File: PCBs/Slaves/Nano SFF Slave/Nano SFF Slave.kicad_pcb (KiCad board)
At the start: 2 copper layers, 52.4 x 50 mm, 52 parts, among them J1 Screw_Terminal_01x02, J10 AVR-ISP-6, J11 Conn_01x06_Female, J12 Screw_Terminal_01x02, J13 Screw_Terminal_01x02, J14 Screw_Terminal_01x02, J15 Screw_Terminal_01x02, J16 Screw_Terminal_01x02, J2 Screw_Terminal_01x02, J3 Screw_Terminal_01x02, J4 Screw_Terminal_01x02, J5 Screw_Terminal_01x02, J6 Screw_Terminal_01x02, J7 Screw_Terminal_01x02, J8 Screw_Terminal_01x02, J9 Screw_Terminal_01x02, SW1 SW_DIP_x02, SW2 SW_DIP_x02, SW3 SW_MEC_5E, U1 ATmega328P-AU, U2 MAX487ESA+T, U3 ULN2003A, U4 MAX487CPA+, U5 AMS1117-5.0, Y1 Crystal_GND24

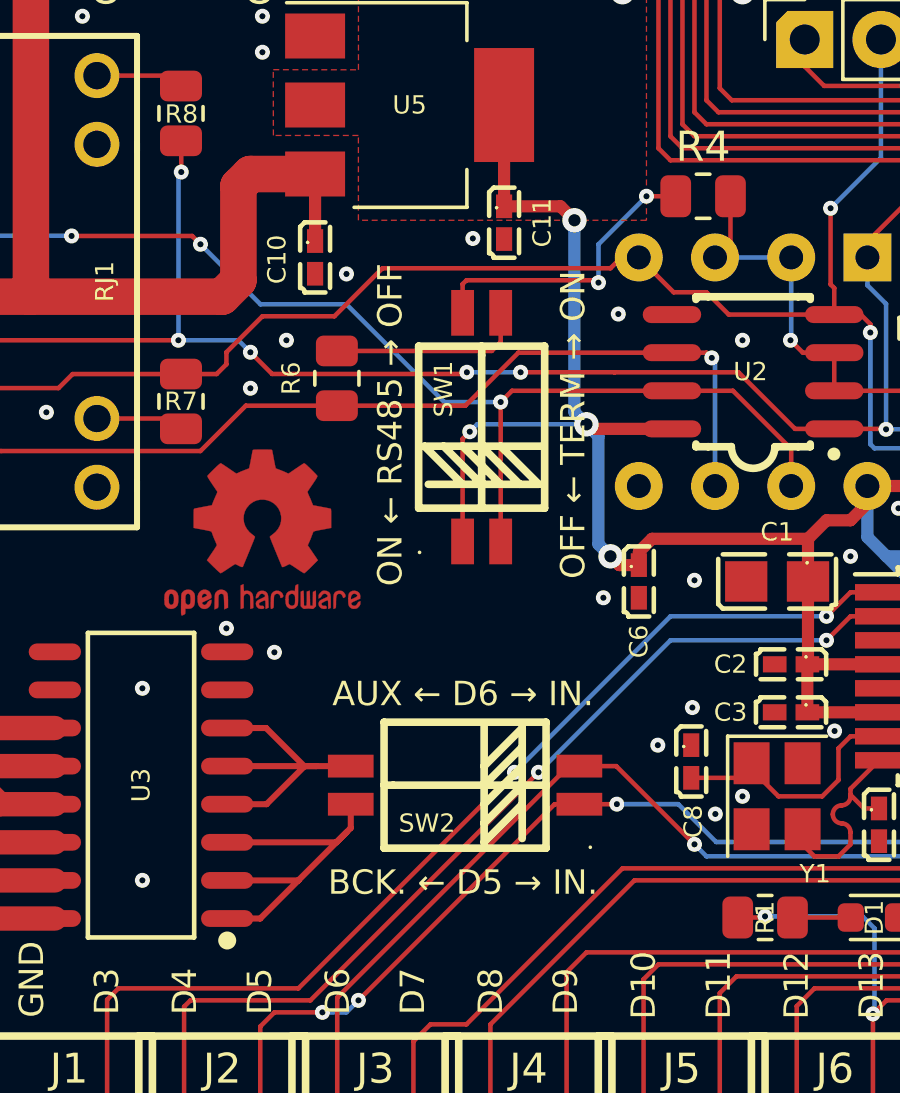
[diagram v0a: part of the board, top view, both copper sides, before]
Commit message: Updated Nano SFF Slave RS485 Switch and Silkscreen
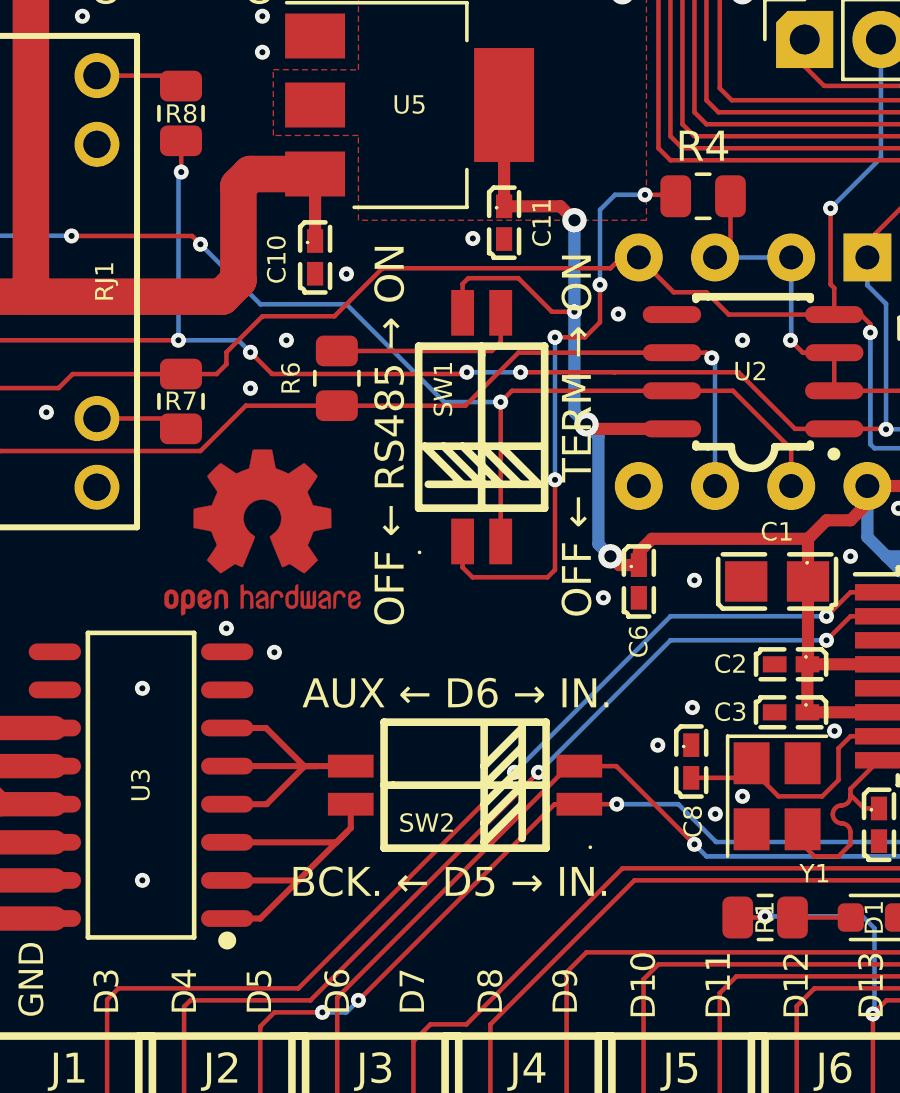
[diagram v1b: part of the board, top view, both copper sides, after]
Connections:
- R4 pad 1: Net-(SW1-Pad4) -> Net-(R4-Pad1)
- SW1 pad 1: +5V -> Net-(R4-Pad1)
- SW1 pad 4: Net-(SW1-Pad4) -> +5V
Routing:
- net Net-(R4-Pad1): track 0.00 -> 20.1 mm, vias 0 -> 4
- net Net-(SW1-Pad4): track 10.1 -> 0.00 mm, vias 2 -> 0
- net +5V: track 115.6 -> 113.1 mm
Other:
- board text added: "OFF ← RS485 → ON"
- board text removed: "ON ← RS485 → OFF"

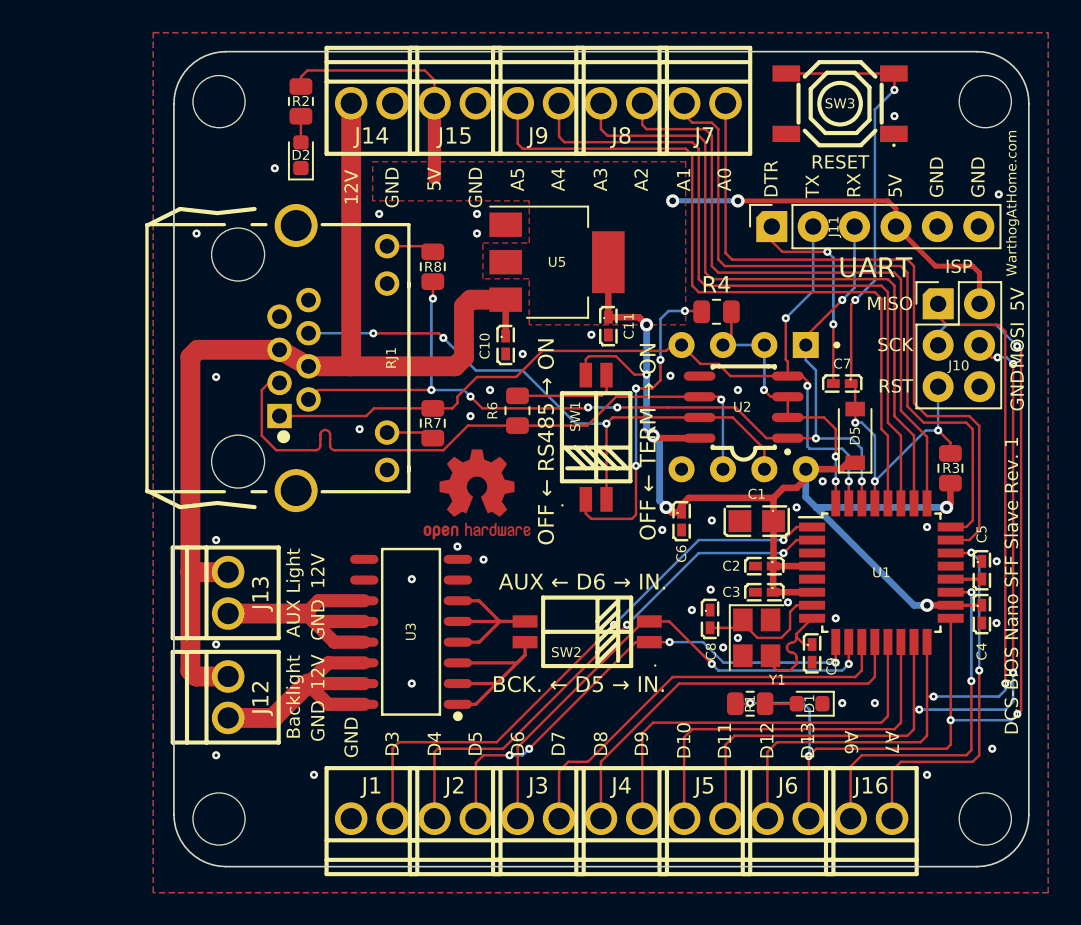
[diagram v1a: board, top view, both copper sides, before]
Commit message: Improved Nano SFF Silkscreen
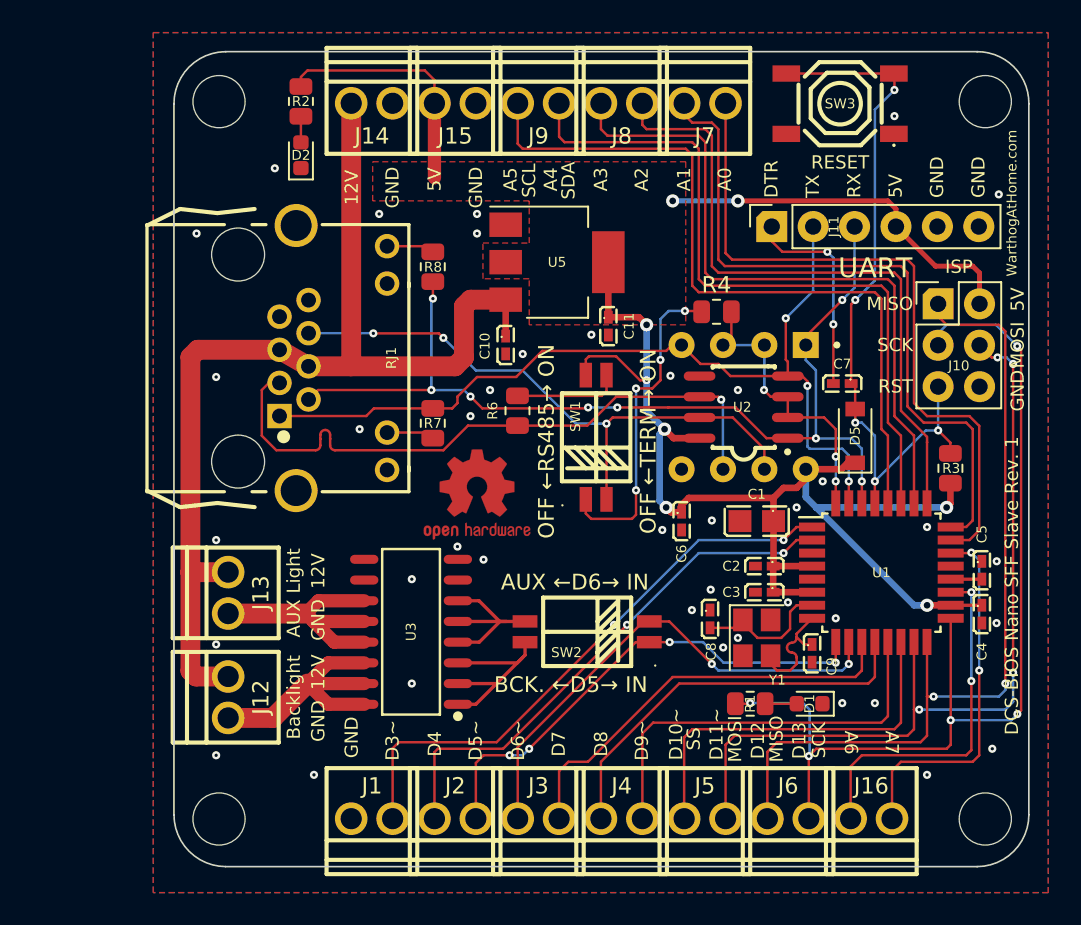
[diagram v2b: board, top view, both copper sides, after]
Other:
- board text added: "AUX ←D6→ IN"
- board text added: "BCK. ←D5→ IN"
- board text added: "OFF ←RS485→ ON"
- board text added: "OFF ←TERM→ ON"
- board text removed: "AUX ← D6 → IN."
- board text removed: "BCK. ← D5 → IN."
- board text removed: "OFF ← RS485 → ON"
- board text removed: "OFF ← TERM → ON"

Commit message: Nano SFF with DS4560S-AR+ hotplug protection (Not Orderable)
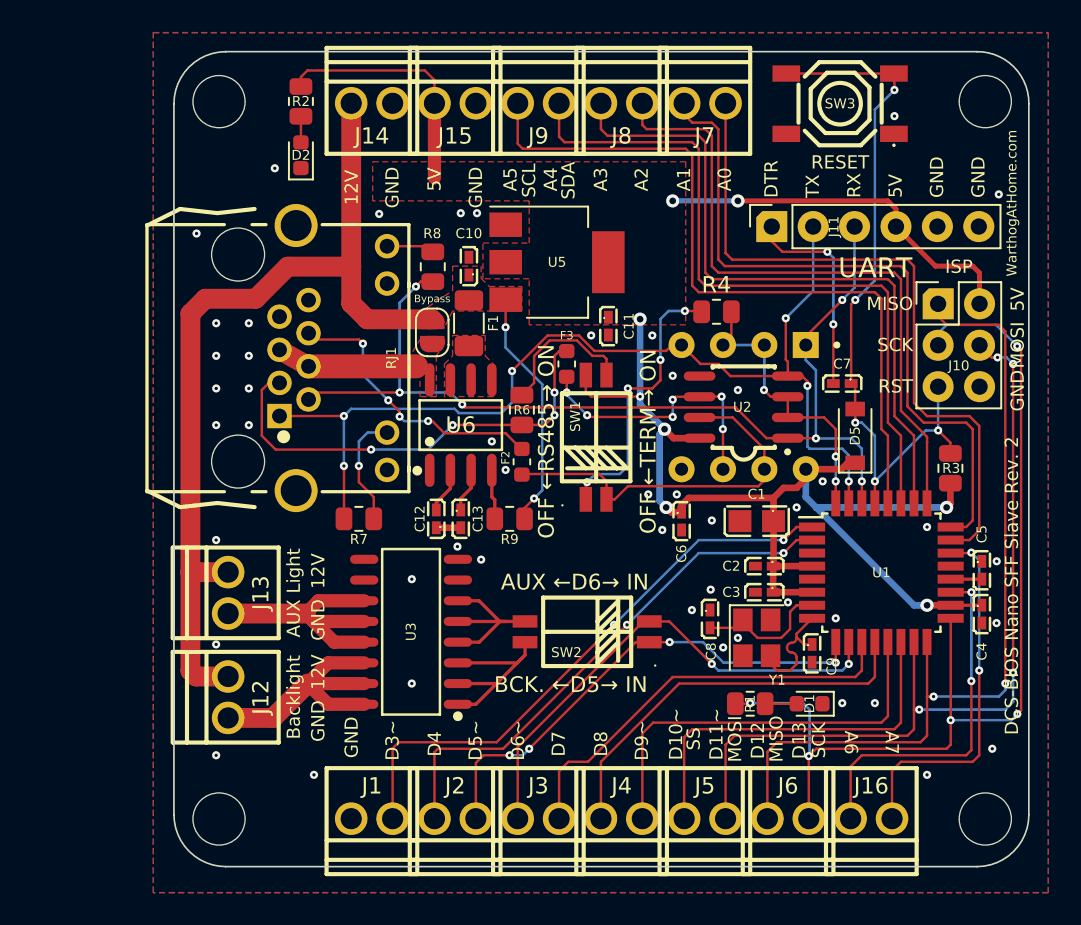
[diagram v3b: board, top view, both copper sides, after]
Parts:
- removed REF**: OSHW-Logo2_7.3x6mm_Copper, Symbol:OSHW-Logo2_7.3x6mm_Copper
- added C12: 5uF, A10 KiCad Libraries:C0402, F.Cu at (118.3, 108.6)
- added C13: 1uF, A10 KiCad Libraries:C0402, F.Cu at (119.8, 108.6)
- added F1: 500mA, Fuse:Fuse_1206_3216Metric, F.Cu at (120.3, 96.6)
- added F2: 100mA, Fuse:Fuse_0603_1608Metric, F.Cu at (123.6, 105.1)
- added F3: 100mA, Fuse:Fuse_0603_1608Metric, F.Cu at (126.3, 99.1)
- added JP1: Bypass, Jumper:SolderJumper-2_P1.3mm_Open_RoundedPad1.0x1.5mm, F.Cu at (118.1, 97.2)
- added R9: 390R, Resistor_SMD:R_0805_2012Metric, F.Cu at (122.8, 108.6)
- added U6: DS4560S-AR+, A10 KiCad Libraries:SOIC-8_L4.9-W3.9-P1.27-LS6.0-BL, F.Cu at (119.8, 102.8)
- moved R7 7.41 mm to (113.6, 108.6), turned to 180 degrees
- moved C10 5.34 mm to (120.3, 93.1), turned to 90 degrees
- moved R6 0.27 mm to (123.6, 101.9)
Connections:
- C10 pad 1: +12V -> LOAD
- J12 pad 2: +12V -> LOAD
- J13 pad 2: +12V -> LOAD
- J14 pad 1: +12V -> LOAD
- SW1 pad 2: RS485- -> URS485-
- U2 pad 6: RS485+ -> Net-(U2-Pad6)
- U2 pad 7: RS485- -> URS485-
- U4 pad 6: RS485+ -> Net-(U2-Pad6)
- U4 pad 7: RS485- -> URS485-
- U5 pad 3: +12V -> LOAD
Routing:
- net LOAD: track 0.00 -> 70.2 mm, vias 0 -> 2
- net +12V: track 65.7 -> 8.65 mm
- net URS485-: track 0.00 -> 23.4 mm
- net RS485-: track 37.1 -> 17.3 mm, vias 3 -> 4
- net Net-(U2-Pad6): track 0.00 -> 16.8 mm, vias 0 -> 6
- net RS485+: track 40.3 -> 27.8 mm, vias 1 -> 4
- net TXD: track 55.0 -> 63.2 mm, vias 3 -> 6
- net +5V: track 113.0 -> 106.6 mm
- net Net-(R7-Pad1): track 2.94 -> 7.08 mm, vias 0 -> 1
- net Net-(R9-Pad2): track 0.00 -> 3.05 mm
- net Net-(C12-Pad2): track 0.00 -> 2.79 mm
- net Net-(C13-Pad1): track 0.00 -> 2.70 mm
- net Net-(R4-Pad1): track 20.1 -> 17.5 mm
- net Net-(R6-Pad2): track 6.56 -> 9.01 mm
- net GND: track 0.00 -> 1.50 mm, vias 40 -> 48
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- added copper zone on F.Cu, net +12V
- added copper zone on F.Cu, net /ULOAD
- added copper zone on F.Cu, net LOAD

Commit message: Nano SFF With Hotplug and RS485 Protection
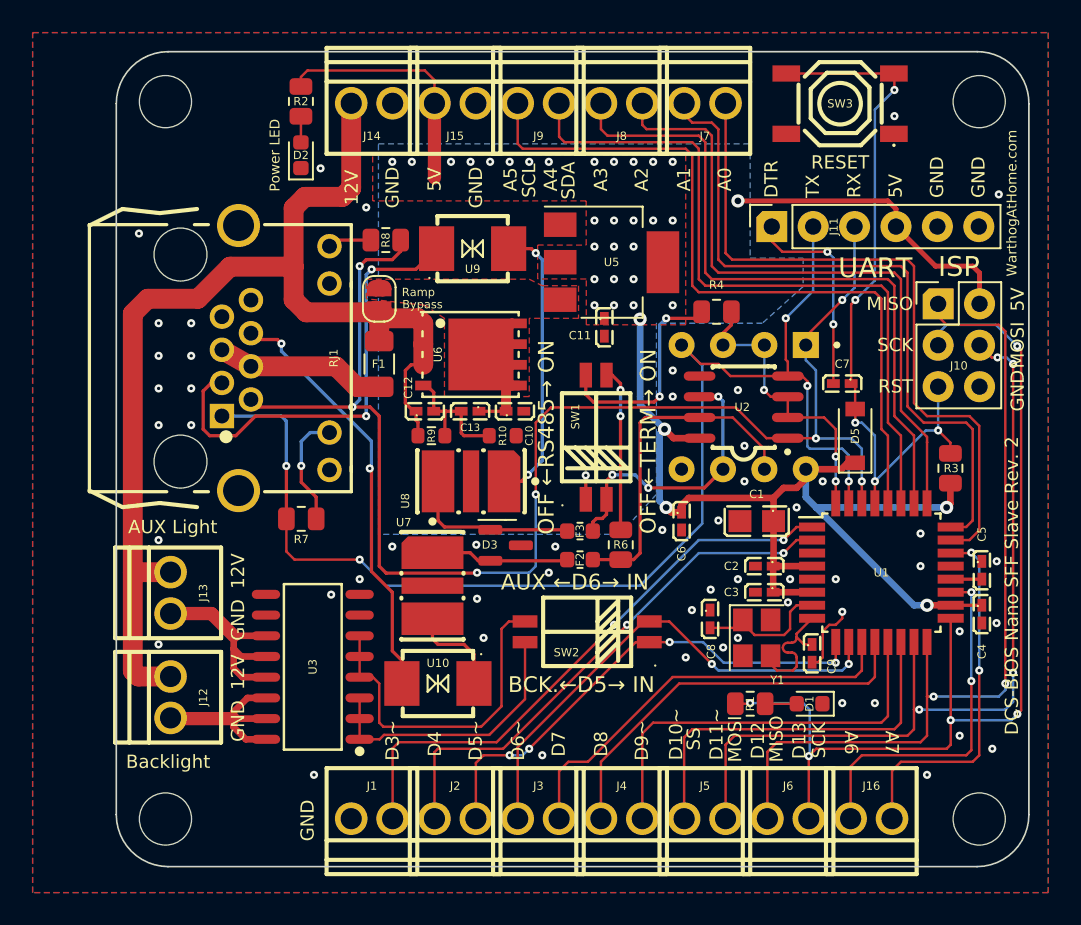
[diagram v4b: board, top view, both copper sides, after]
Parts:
- added D3: SM712_SOT23, Package_TO_SOT_SMD:SOT-23, F.Cu at (122.6, 110.2)
- added R10: 1M, Resistor_SMD:R_0603_1608Metric, F.Cu at (122.4, 103.5)
- added U10: TISP4240M3BJR-S, A10 KiCad Libraries:DO-214AA_L4.4-W3.6-LS5.3-BI, F.Cu at (118.4, 118.7)
- added U7: TBU-CA065-200-WH, A10 KiCad Libraries:DIO-SMD_3P-L6.5-W4.0-BI, F.Cu at (118.1, 112.7)
- added U8: TBU-CA065-200-WH, A10 KiCad Libraries:DIO-SMD_3P-L6.5-W4.0-BI, F.Cu at (120.5, 106.3)
- added U9: TISP4240M3BJR-S, A10 KiCad Libraries:DO-214AA_L4.4-W3.6-LS5.3-BI, F.Cu at (120.6, 92.0)
- C12: value 5uF -> 500nF
- C13: value 1uF -> 50nF
- JP1: value Bypass -> Solder
- R9: value 390R -> 10M; footprint Resistor_SMD:R_0805_2012Metric -> Resistor_SMD:R_0603_1608Metric
- U6: value DS4560S-AR+ -> HY15P03C2; footprint A10 KiCad Libraries:SOIC-8_L4.9-W3.9-P1.27-LS6.0-BL -> A10 KiCad Libraries:DFN-8_L5.9-W5.2-P1.27-LS6.2-BL
- moved F3 10.3 mm to (127.1, 109.3), turned to 0 degrees
- moved R6 10.2 mm to (129.6, 110.2)
- moved C10 9.34 mm to (123.2, 102.0), turned to 0 degrees
- moved R9 7.00 mm to (118.0, 103.5), turned to 0 degrees
- moved F2 6.98 mm to (127.1, 111.1), turned to 180 degrees
- moved C12 6.64 mm to (117.6, 102.0), turned to 0 degrees
- moved C13 6.62 mm to (120.4, 102.0), turned to 180 degrees
- moved U3 6.40 mm to (110.8, 117.7)
- moved F1 6.04 mm to (114.8, 99.1)
- moved U6 4.38 mm to (120.4, 98.5), turned to -90 degrees
- moved JP1 3.88 mm to (114.8, 95.1)
- moved J12 3.53 mm to (101.9, 119.5)
- moved J13 3.53 mm to (101.9, 113.1)
- moved R7 3.53 mm to (110.0, 108.6)
- moved RJ1 3.53 mm to (105.1, 98.7)
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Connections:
- C10 pad 1: LOAD -> 12V_Ramped
- C12 pad 1: GND -> 12V_Fused
- C13 pad 1: Net-(C13-Pad1) -> 12V_Ramped
- C13 pad 2: GND -> Net-(C12-Pad2)
- F1 pad 1: LOAD -> 12V_Fused
- F1 pad 2: /ULOAD -> +12V
- F2 pad 1: URS485- -> TERM_B
- F2 pad 2: RS485- -> Net-(D3-Pad2)
- F3 pad 1: Net-(U2-Pad6) -> Net-(D3-Pad1)
- F3 pad 2: RS485+ -> TERM_A
- J12 pad 2: LOAD -> 12V_Fused
- J13 pad 2: LOAD -> 12V_Fused
- J14 pad 1: LOAD -> 12V_Fused
- JP1 pad 1: +12V -> 12V_Fused
- JP1 pad 2: LOAD -> 12V_Ramped
- R6 pad 1: RS485+ -> TERM_B
- R9 pad 1: LOAD -> 12V_Fused
- R9 pad 2: Net-(R9-Pad2) -> Net-(C12-Pad2)
- SW1 pad 1: Net-(R4-Pad1) -> +5V
- SW1 pad 2: URS485- -> TERM_A
- SW1 pad 4: +5V -> Net-(R4-Pad1)
- U2 pad 6: Net-(U2-Pad6) -> TERM_A
- U2 pad 7: URS485- -> TERM_B
- U4 pad 6: Net-(U2-Pad6) -> TERM_A
- U4 pad 7: URS485- -> TERM_B
- U5 pad 3: LOAD -> 12V_Ramped
- U6 pad 1: GND -> 12V_Fused
- U6 pad 2: Net-(C12-Pad2) -> 12V_Fused
- U6 pad 3: Net-(C13-Pad1) -> 12V_Fused
- U6 pad 4: Net-(R9-Pad2) -> Net-(C12-Pad2)
- U6 pad 5: /ULOAD -> 12V_Ramped
- U6 pad 6: /ULOAD -> 12V_Ramped
- U6 pad 7: /ULOAD -> 12V_Ramped
- U6 pad 8: +12V -> 12V_Ramped
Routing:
- net 12V_Fused: track 0.00 -> 71.3 mm
- net LOAD: track 70.2 -> 0.00 mm, vias 2 -> 0
- net RXD: track 61.5 -> 87.9 mm, vias 6 -> 7
- net URS485-: track 23.4 -> 0.00 mm
- net TERM_B: track 0.00 -> 20.9 mm
- net Net-(U8-Pad1): track 0.00 -> 17.5 mm, vias 0 -> 2
- net TERM_A: track 0.00 -> 17.5 mm, vias 0 -> 3
- net Net-(U2-Pad6): track 16.8 -> 0.00 mm, vias 6 -> 0
- net TXD: track 63.2 -> 79.8 mm, vias 6 -> 5
- net Net-(D3-Pad1): track 0.00 -> 10.6 mm
- net AUX_BASE: track 10.7 -> 20.8 mm
- net RS485-: track 17.3 -> 26.1 mm, vias 4 -> 2
- net Net-(D3-Pad2): track 0.00 -> 8.50 mm
- net +5V: track 106.6 -> 99.7 mm, vias 8 -> 35
- net Net-(U10-Pad1): track 0.00 -> 5.97 mm
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- added copper zone on B.Cu, net +5V
- added copper zone on F.Cu, net 12V_Ramped
- removed copper zone on F.Cu, net +12V
- removed copper zone on F.Cu, net /ULOAD
- removed copper zone on F.Cu, net LOAD
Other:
- board size 52.4 x 50 mm -> 56 x 50 mm
- board text added: "BCK.←D5→ IN"
- board text removed: "BCK. ←D5→ IN"
